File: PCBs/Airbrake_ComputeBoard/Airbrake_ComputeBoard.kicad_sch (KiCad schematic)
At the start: 28 parts, among them Q1 Q_NPN_BEC, Q2 Q_NPN_BEC, Q3 Q_NPN_BEC, Q4 Q_NPN_BEC

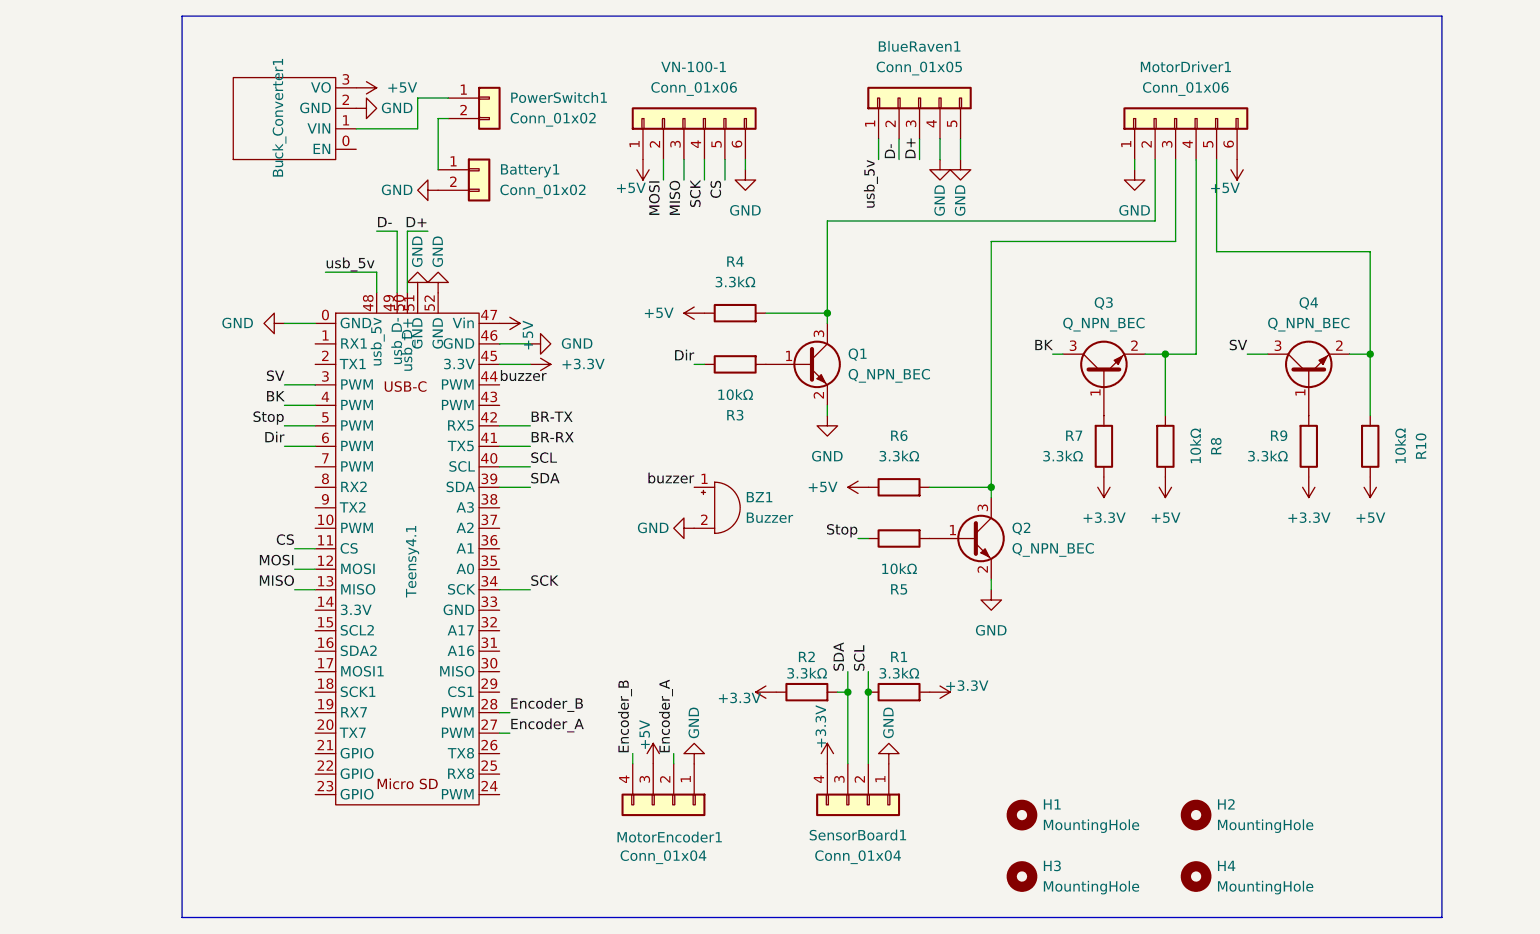
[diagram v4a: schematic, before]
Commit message: Added optocouplers, level shifter, and connector for a limit switch
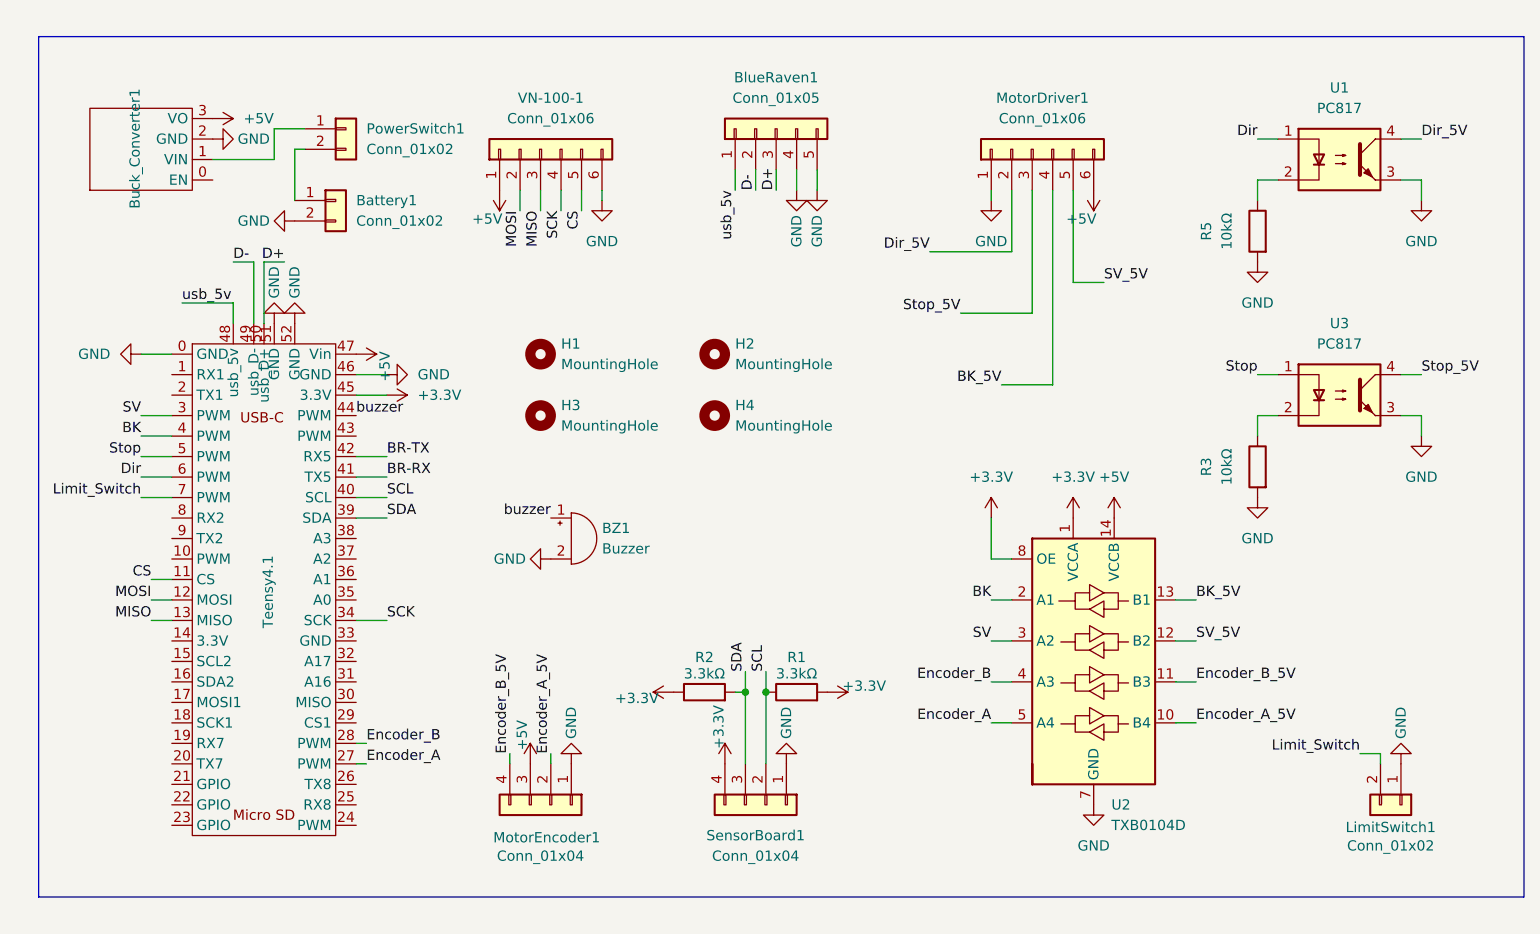
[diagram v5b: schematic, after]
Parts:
- removed Q1, Q2, Q3, Q4: Q_NPN_BEC, Package_TO_SOT_SMD:SOT-23, symbol Device:Q_NPN_BEC
- removed R10, R8: 10kΩ, Resistor_SMD:R_0805_2012Metric_Pad1.20x1.40mm_HandSolder, symbol Device:R
- removed R4, R6, R7, R9: 3.3kΩ, Resistor_SMD:R_0805_2012Metric_Pad1.20x1.40mm_HandSolder, symbol Device:R
- added LimitSwitch1: Conn_01x02, symbol Connector_Generic:Conn_01x02
- added U1, U3: PC817, Package_DIP:DIP-4_W7.62mm, symbol Isolator:PC817
- added U2: TXB0104D, Package_SO:SOIC-14_3.9x8.7mm_P1.27mm, symbol Logic_LevelTranslator:TXB0104D
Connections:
- net +3.3V: now also U2.1 (VCCA), U2.8 (OE)
- net +5V: now also U2.14 (VCCB)
- net BK: now also U2.2 (A1)
- net Dir: now also U1.1; no longer R3.1
- net Encoder_A: now also U2.5 (A4); no longer MotorEncoder1.2 (Pin_2)
- net Encoder_B: now also U2.4 (A3); no longer MotorEncoder1.4 (Pin_4)
- net GND: now also R3.2, R5.2, LimitSwitch1.1 (Pin_1), U1.3, U2.7 (GND), U3.3
- net SV: now also U2.3 (A2)
- net Stop: now also U3.1; no longer R5.1
- net BK_5V: now reaches MotorDriver1.4 (Pin_4)
- net BK_5V: now also U2.13 (B1)
- net SV_5V: now reaches MotorDriver1.5 (Pin_5)
- net SV_5V: now also U2.12 (B2)
- net Dir_5V: now reaches MotorDriver1.2 (Pin_2)
- net Dir_5V: now also U1.4
- net Limit_Switch: now reaches Teensy4.1.7 (PWM)
- net Limit_Switch: now also LimitSwitch1.2 (Pin_2)
- net Stop_5V: now reaches MotorDriver1.3 (Pin_3)
- net Stop_5V: now also U3.4
- new net: R3.1, U3.2
- new net: R5.1, U1.2
- new net Encoder_A_5V: MotorEncoder1.2 (Pin_2), U2.10 (B4)
- new net Encoder_B_5V: MotorEncoder1.4 (Pin_4), U2.11 (B3)
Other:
- moved on the sheet: BZ1, Battery1, BlueRaven1, Buck_Converter1, H1, H2, H3, H4, MotorDriver1, MotorEncoder1, PowerSwitch1, R1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

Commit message: Made new PCB
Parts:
- added C1, C2: 0.1µF, Capacitor_SMD:C_0805_2012Metric_Pad1.18x1.45mm_HandSolder, symbol Device:C
- LimitSwitch1: footprint (none) -> Connector_JST:JST_XH_B2B-XH-A_1x02_P2.50mm_Vertical
- R3, R5: value 10kΩ -> 180Ω
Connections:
- net +3.3V: now also C1.1
- net +5V: now also C2.1
- net BK: now also U2.4 (A3); no longer U2.2 (A1)
- net BK_5V: now also U2.11 (B3); no longer U2.13 (B1)
- net Encoder_A: now also U2.2 (A1); no longer U2.5 (A4)
- net Encoder_A_5V: now also U2.13 (B1); no longer U2.10 (B4)
- net Encoder_B: now also U2.3 (A2); no longer U2.4 (A3)
- net Encoder_B_5V: now also U2.12 (B2); no longer U2.11 (B3)
- net GND: now also C1.2, C2.2
- net SV: now also U2.5 (A4); no longer U2.3 (A2)
- net SV_5V: now also U2.10 (B4); no longer U2.12 (B2)
